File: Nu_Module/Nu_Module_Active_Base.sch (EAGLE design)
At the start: 3 parts

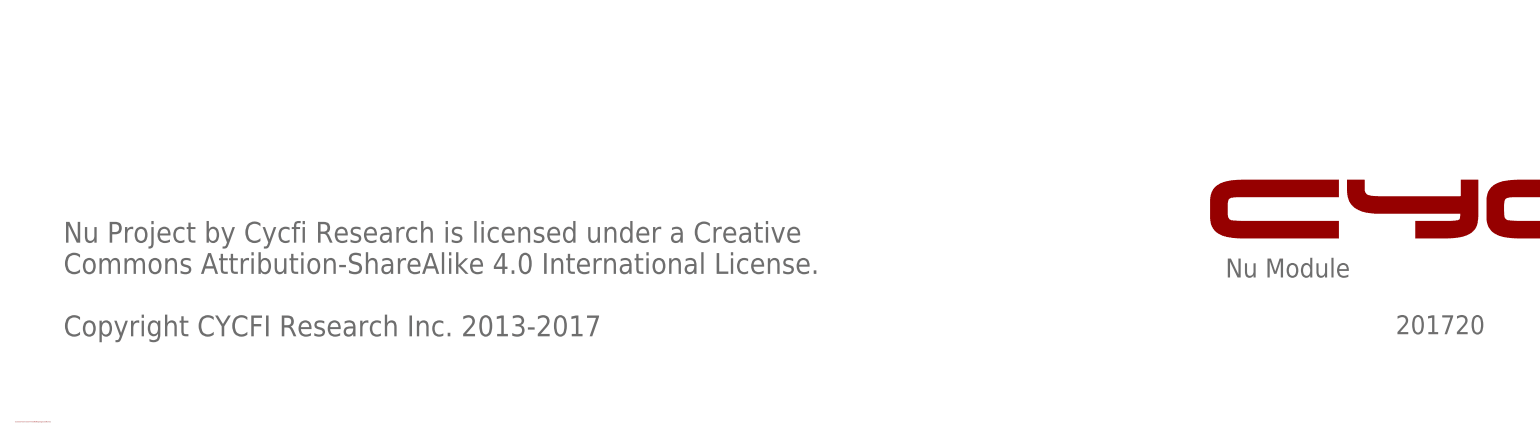
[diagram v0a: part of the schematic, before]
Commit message: Updated Notes "For Nu Project" instead of "Nexus"
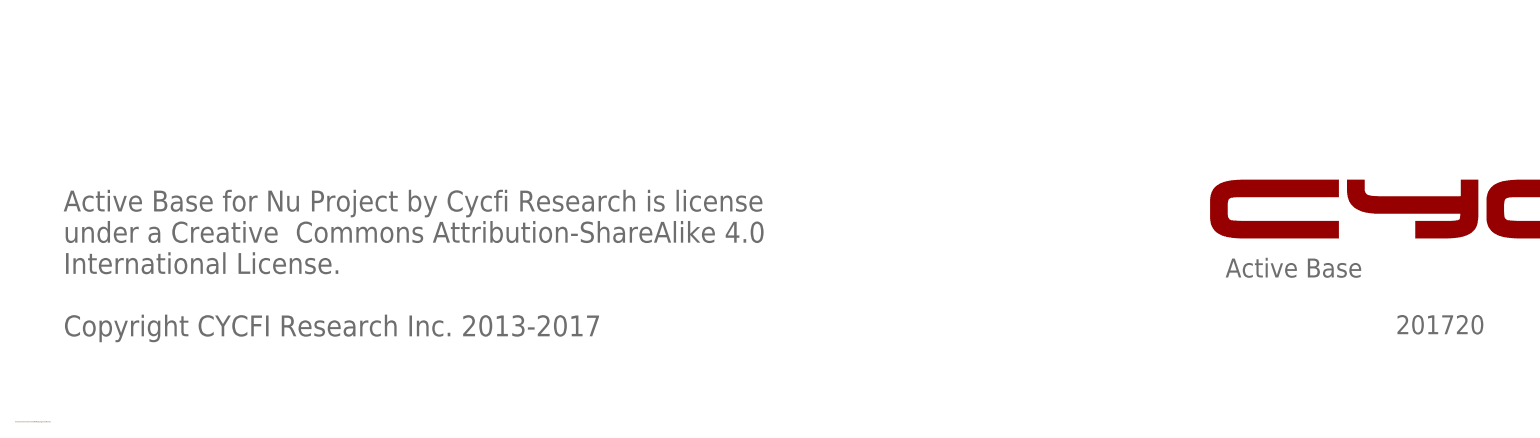
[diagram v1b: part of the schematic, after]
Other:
- note added: "Active Base"
- note added: "Active Base for Nu Project by Cycfi Research is license under a Creative Commons Attribution-ShareAlike 4.0 International License. Copyright CYCFI Research Inc. 2013-2017"
- note removed: "Nu Module"
- note removed: "Nu Project by Cycfi Research is licensed under a Creative Commons Attribution-ShareAlike 4.0 International License. Copyright CYCFI Research Inc. 2013-2017"
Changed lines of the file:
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@@
 <text x="158.115" y="-2.54" size="1.778" layer="95">VCC</text>
 <text x="158.115" y="-5.08" size="1.778" layer="95">GND</text>
-<text x="193.04" y="-85.09" size="2.54" layer="95">Nu Module</text>
+<text x="193.04" y="-85.09" size="2.54" layer="95">Active Base</text>
 <text x="267.97" y="-97.155" size="2.1844" layer="95">v0.94</text>
-<text x="37.0078" y="-92.9894" size="2.794" layer="95">Nu Project by Cycfi Research is licensed under a Creative
-Commons Attribution-ShareAlike 4.0 International License.
+<text x="37.0078" y="-92.9894" size="2.794" layer="95">Active Base for Nu Project by Cycfi Research is license
+under a Creative  Commons Attribution-ShareAlike 4.0
+International License.
 Copyright CYCFI Research Inc. 2013-2017</text>
 <text x="30.48" y="-104.52735" size="0.154940625" layer="94" font="vector">C:/Users/mark belarmino/Desktop/Logo-2016.bmp</text>

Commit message: Updated document number.
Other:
- note added: "2017020"
- note removed: "201720"
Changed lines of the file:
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@@
 <text x="158.115" y="-5.08" size="1.778" layer="95">GND</text>
 <text x="193.04" y="-85.09" size="2.54" layer="95">Active Base</text>
-<text x="267.97" y="-97.155" size="2.1844" layer="95">v0.94</text>
-<text x="37.0078" y="-92.9894" size="2.794" layer="95">Active Base for Nu Project by Cycfi Research is license
-under a Creative  Commons Attribution-ShareAlike 4.0
-International License.
+<text x="267.97" y="-97.155" size="2.54" layer="95">v0.94</text>
+<text x="37.0078" y="-92.9894" size="2.54" layer="95">Active Base for Nu Project by Cycfi Research is license under
+a Creative  Commons Attribution-ShareAlike 4.0 International
+License.
 Copyright CYCFI Research Inc. 2013-2017</text>
 <text x="30.48" y="-104.52735" size="0.154940625" layer="94" font="vector">C:/Users/mark belarmino/Desktop/Logo-2016.bmp</text>
@@
 <rectangle x1="264.155553125" y1="-71.963915625" x2="266.511403125" y2="-71.955028125" layer="94"/>
 <text x="147.955" y="-22.86" size="1.778" layer="95">H2</text>
-<text x="215.9" y="-92.71" size="2.54" layer="95">201720</text>
+<text x="215.9" y="-92.71" size="2.54" layer="95">2017020</text>
 </plain>
 <instances>
